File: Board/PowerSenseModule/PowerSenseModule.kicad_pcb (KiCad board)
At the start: 2 copper layers, 49 parts, among them J1 Conn_01x06_Male, J3 Programming Header, J4 Conn_01x02_Male, U1 TPS82150, U2 NCV2007x, U3 dsPIC33EV32GM102, U4 MCP2542FDxMF

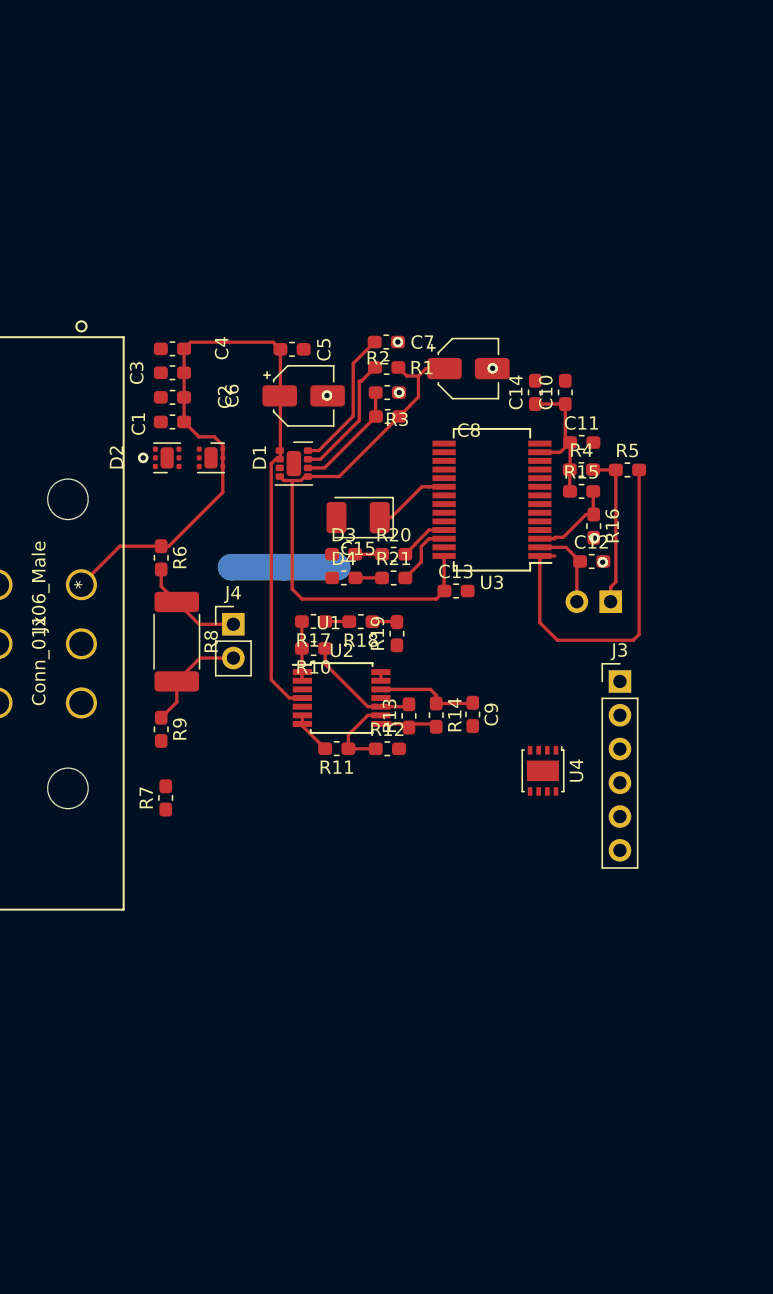
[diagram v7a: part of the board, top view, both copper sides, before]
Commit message: Design changes/comments
Reorienting everything to keep power traces and signal traces seperate as possible
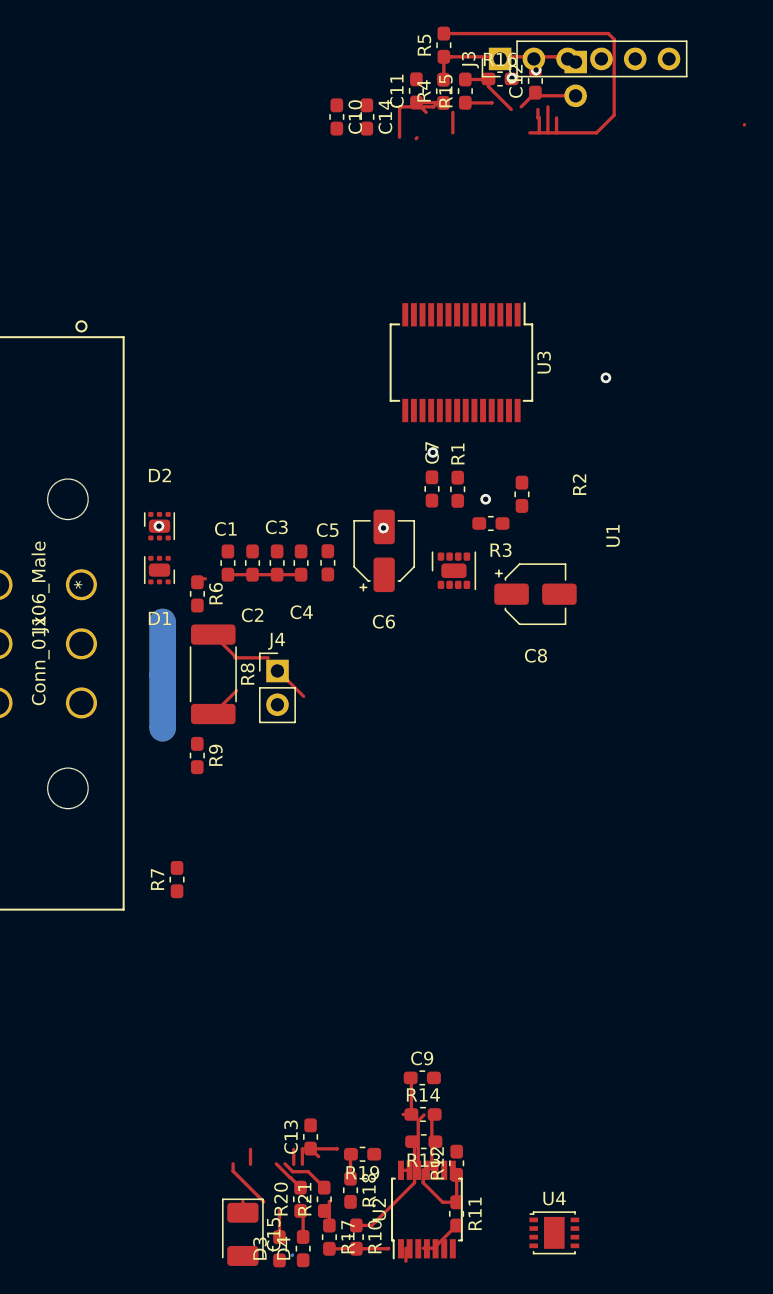
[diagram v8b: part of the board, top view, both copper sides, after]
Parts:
- moved C15 54.6 mm to (160.1, 136.7), turned to 270 degrees
- moved D3 52.5 mm to (162.9, 137.8), turned to 90 degrees
- moved D4 50.5 mm to (164.7, 137.8), turned to 90 degrees
- moved R20 49.0 mm to (164.5, 134.0), turned to 90 degrees
- moved J3 47.7 mm to (179.5, 48.3), turned to 90 degrees
- moved R21 47.0 mm to (166.3, 134.0), turned to 90 degrees
- moved R17 46.3 mm to (166.6, 136.9), turned to 270 degrees
- moved R10 44.4 mm to (168.7, 136.9), turned to 270 degrees
- moved R18 42.8 mm to (168.2, 133.4), turned to 270 degrees
- moved C13 42.5 mm to (165.2, 129.4), turned to 90 degrees
- moved JP1 40.7 mm to (185.2, 48.5), turned to 180 degrees
- moved R19 39.2 mm to (169.1, 130.7), turned to 180 degrees
- moved U2 39.0 mm to (174.0, 134.8), turned to 90 degrees
- moved C12 36.4 mm to (182.1, 49.9), turned to 90 degrees
- moved R11 36.1 mm to (176.2, 135.1), turned to 270 degrees
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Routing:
- net +12V: track 62.1 -> 7.05 mm
- net +5V: track 53.2 -> 15.8 mm
- net Net-(C7-Pad1): track 10.7 -> 0.00 mm
- net Net-(R1-Pad2): track 9.77 -> 0.00 mm
- net Net-(R2-Pad2): track 8.53 -> 0.00 mm
- net Net-(J4-Pad2): track 8.20 -> 2.49 mm
- net Net-(R5-Pad2): track 26.7 -> 30.5 mm
- net Net-(C12-Pad1): track 6.59 -> 4.63 mm
- net Net-(R15-Pad2): track 6.61 -> 4.76 mm
- net GNDD: track 0.08 -> 1.70 mm
- net Net-(U3-Pad23): track 0.00 -> 1.12 mm
- net Net-(R21-Pad2): track 4.82 -> 3.70 mm
- net Net-(R20-Pad2): track 3.69 -> 2.57 mm
- net Net-(C15-Pad1): track 5.80 -> 4.67 mm
- net Net-(J4-Pad1): track 7.88 -> 6.81 mm
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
